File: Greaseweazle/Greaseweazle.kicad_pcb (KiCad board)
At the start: 2 copper layers, 90 x 94 mm, 17 parts, among them J1 FDC_PC, J2 PWR_EXT1, J3 PWR_DRV, J4 PWR_EXT2, J5 USB_TTL, J6 FDC_Amstrad, M1 Mounting, M2 Mounting, M3 Mounting, M4 Mounting

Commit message: Fixed silkscreen error
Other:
- board text added: "PWR_SEL: 1-2 5v barrel jack 2-3 USB"
- board text removed: "PWR_SEL: 1-2 USB 2-3 5v barrel jack"

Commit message: Greaseweazle faceplate with amstrad cutout
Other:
- board text added: "Amiga DrawBridge (Greaseweazle) github.com/tebl"
- board text removed: "Greaseweazle github.com/tebl"

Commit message: Changed power pin order
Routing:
- net Net-(D1-Pad2): track 126.8 -> 128.6 mm
- net Net-(J3-Pad4): track 15.0 -> 16.6 mm
- net GND: track 0.00 -> 1.27 mm

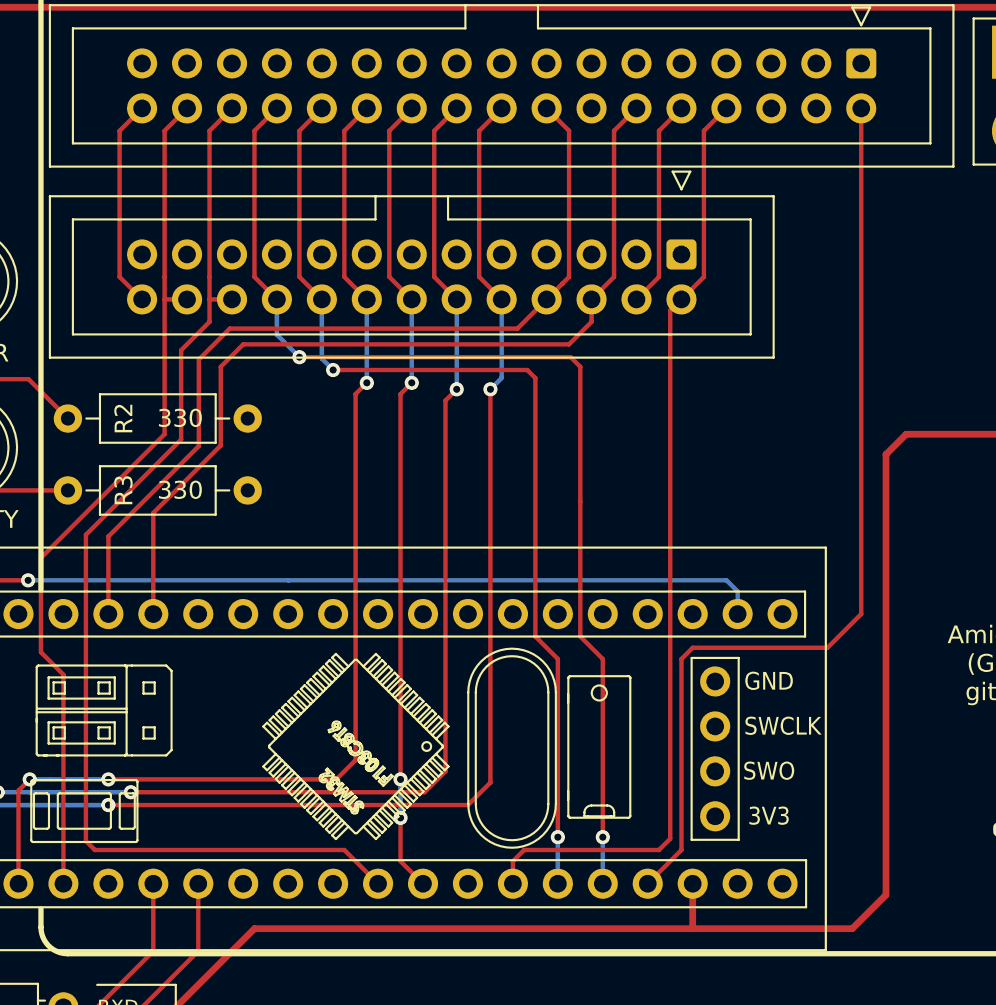
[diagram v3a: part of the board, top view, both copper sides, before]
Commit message: Invert activity LED
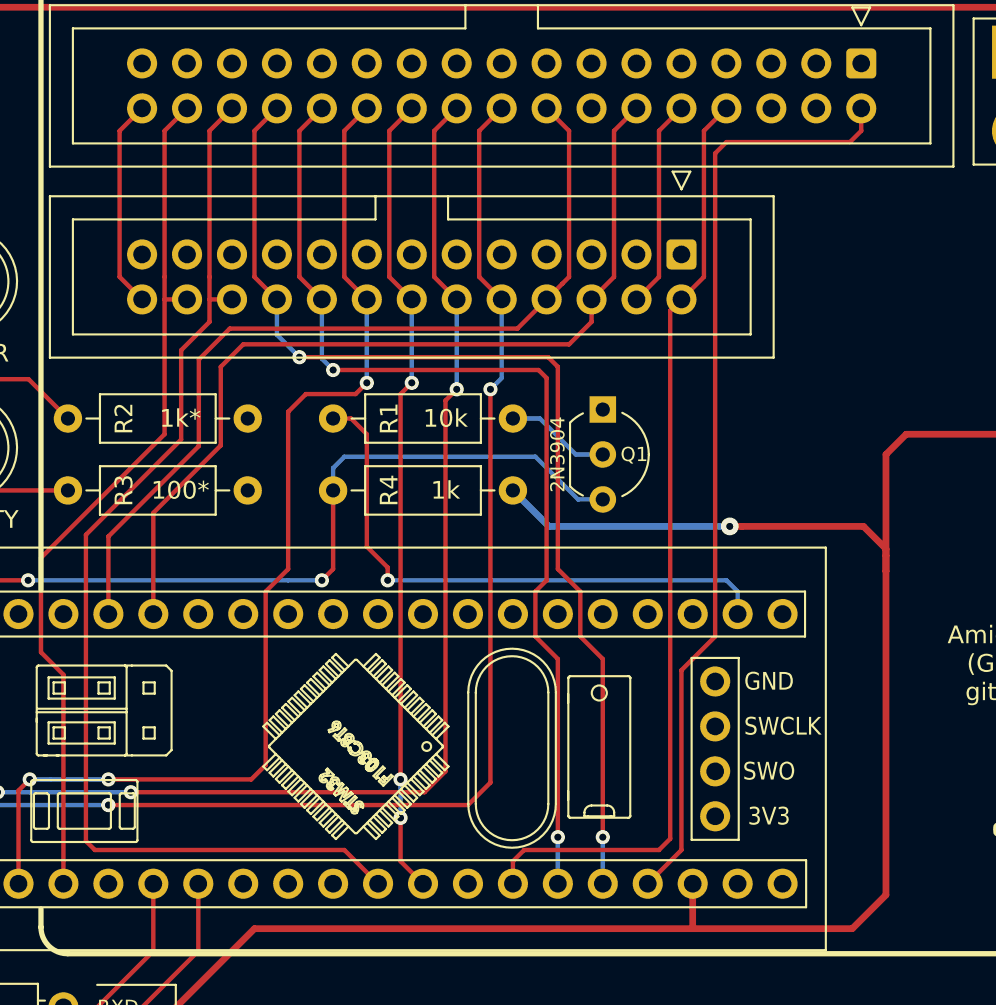
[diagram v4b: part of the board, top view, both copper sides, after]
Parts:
- added Q1: 2N3904, Package_TO_SOT_THT:TO-92_Inline_Wide, F.Cu at (148.6, 79.2)
- added R1: 10k, Resistor_THT:R_Axial_DIN0207_L6.3mm_D2.5mm_P10.16mm_Horizontal, F.Cu at (133.3, 79.8)
- added R4: 1k, Resistor_THT:R_Axial_DIN0207_L6.3mm_D2.5mm_P10.16mm_Horizontal, F.Cu at (143.5, 83.8)
- R2: value 330 -> 1k*
- R3: value 330 -> 100*
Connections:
- D2 pad 2: Net-(A1-Pad22) -> Net-(D2-Pad2)
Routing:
- net Net-(D2-Pad2): track 0.00 -> 55.4 mm, vias 0 -> 2
- net Net-(A1-Pad22): track 57.4 -> 33.0 mm
- net VCC: track 108.8 -> 132.6 mm, vias 0 -> 1
- net Net-(Q1-Pad2): track 0.00 -> 5.92 mm
- net /~WGATE: track 63.2 -> 62.0 mm
- net /~TRK00: track 56.8 -> 57.7 mm
- net /~WPT: track 61.5 -> 60.7 mm
